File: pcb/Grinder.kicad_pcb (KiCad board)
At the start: 4 copper layers, 48 x 73 mm, 32 parts, among them J1 Conn_01x06, J2 Conn_01x05, J3 Conn_01x04, J4 Conn_02x05_Odd_Even, Q1 2N7002, U1 ADS1232IPW, U2 XC6206P502MR

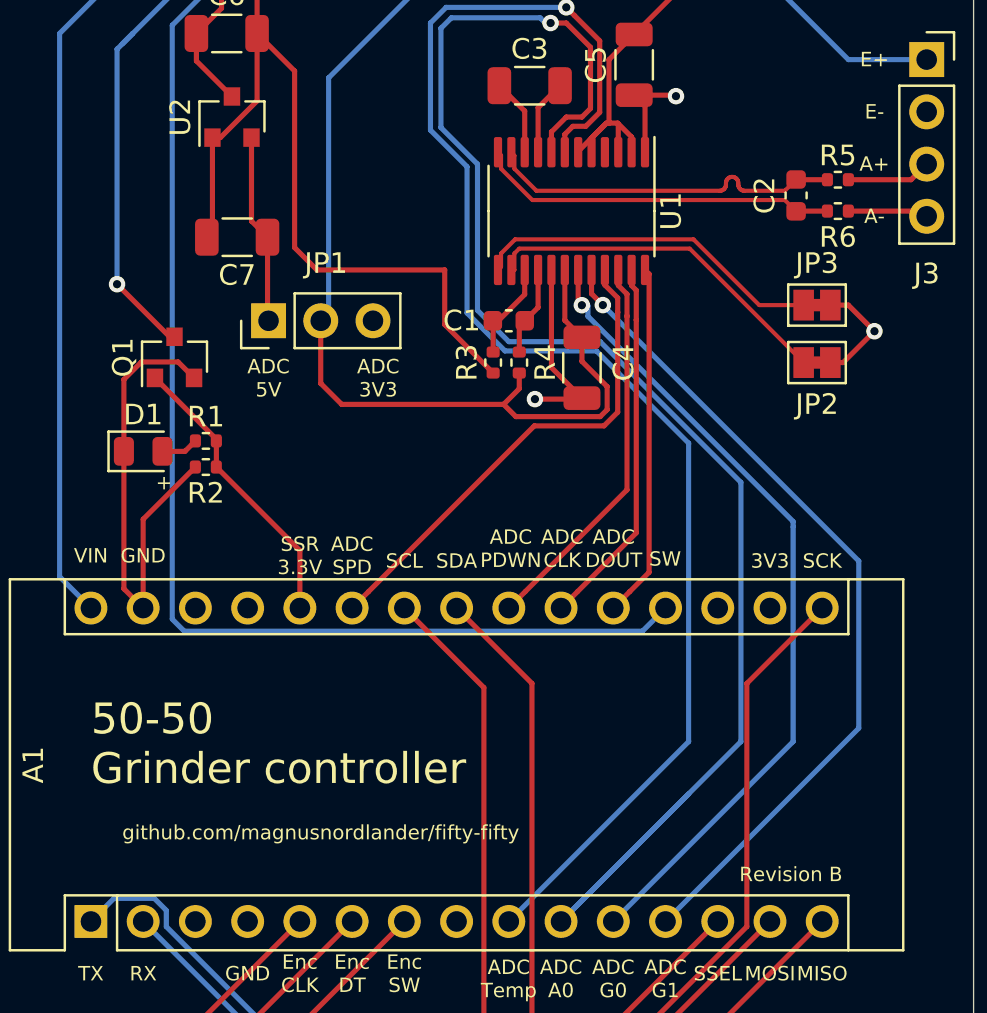
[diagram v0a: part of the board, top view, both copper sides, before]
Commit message: Updated to revision C PCB
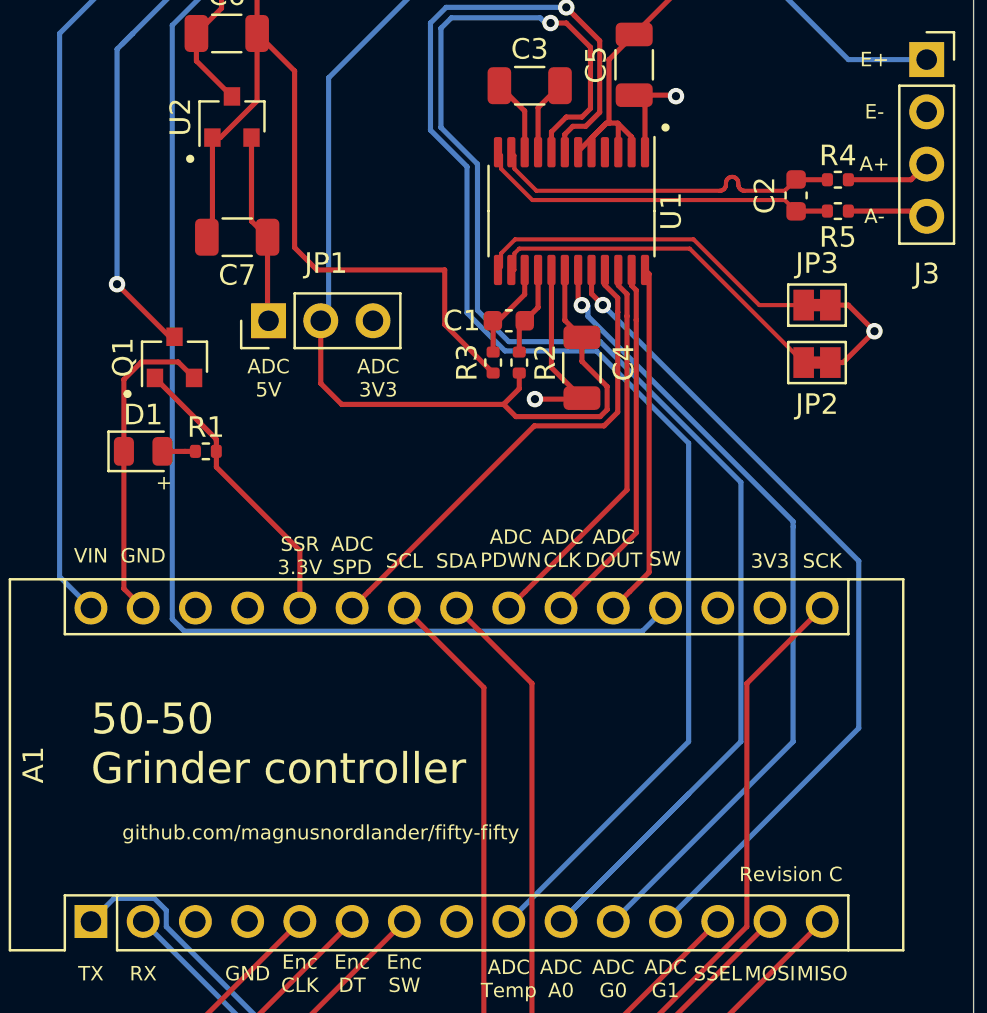
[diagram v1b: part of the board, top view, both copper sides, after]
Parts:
- removed the R2 at (137.7, 78.2)
- moved R1 0.51 mm to (137.7, 77.5)
- renumbered R3 to R2, R4 to R3, R5 to R4, R6 to R5
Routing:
- net GND: track 111.5 -> 103.6 mm
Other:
- board text added: "Revision C"
- board text removed: "Revision B"
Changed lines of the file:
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@@
   (general
     (thickness 1.6)
-    (drawings 89)
-    (tracks 330)
+    (drawings 92)
+    (tracks 328)
     (zones 0)
-    (modules 32)
+    (modules 31)
     (nets 45)
   )
@@
     (tags resistor)
     (attr smd)
-    (fp_text reference R6 (at 0 1.27) (layer F.SilkS)
+    (fp_text reference R5 (at 0 1.27) (layer F.SilkS)
       (effects (font (size 1 1) (thickness 0.15)))
     )
@@
     (tags resistor)
     (attr smd)
-    (fp_text reference R5 (at 0 -1.17) (layer F.SilkS)
+    (fp_text reference R4 (at 0 -1.17) (layer F.SilkS)
       (effects (font (size 1 1) (thickness 0.15)))
     )
@@
     (tags resistor)
     (attr smd)
-    (fp_text reference R4 (at 0 -2.54 90) (layer F.SilkS)
+    (fp_text reference R3 (at 0 1.27 90) (layer F.SilkS)
       (effects (font (size 1 1) (thickness 0.15)))
     )
@@
     (tags resistor)
     (attr smd)
-    (fp_text reference R3 (at 0 2.54 90) (layer F.SilkS)
+    (fp_text reference R2 (at 0 -1.27 90) (layer F.SilkS)
       (effects (font (size 1 1) (thickness 0.15)))
     )
@@
   )
   (module Resistor_SMD:R_0402_1005Metric placed (layer F.Cu)
-    (at 137.668 78.232)
-    (descr "Resistor SMD 0402 (1005 Metric), square (rectangular) end terminal, IPC_7351 nominal, (Body size source: IPC-SM-782 page 72, https://www.pcb-3d.com/wordpress/wp-content/uploads/ipc-sm-782a_amendment_1_and_2.pdf), generated with kicad-footprint-generator")
-    (tags resistor)
-    (attr smd)
-    (fp_text reference R2 (at 0 1.27) (layer F.SilkS)
-      (effects (font (size 1 1) (thickness 0.15)))
-    )
-    (fp_text value 100R (at 0 1.17) (layer F.Fab)
-      (effects (font (size 1 1) (thickness 0.15)))
-    )
-    (fp_line (start -0.525 0.27) (end -0.525 -0.27) (layer F.Fab) (width 0.1))
-    (fp_line (start -0.525 -0.27) (end 0.525 -0.27) (layer F.Fab) (width 0.1))
-    (fp_line (start 0.525 -0.27) (end 0.525 0.27) (layer F.Fab) (width 0.1))
-    (fp_line (start 0.525 0.27) (end -0.525 0.27) (layer F.Fab) (width 0.1))
-    (fp_line (start -0.153641 -0.38) (end 0.153641 -0.38) (layer F.SilkS) (width 0.12))
-    (fp_line (start -0.153641 0.38) (end 0.153641 0.38) (layer F.SilkS) (width 0.12))
-    (fp_line (start -0.93 0.47) (end -0.93 -0.47) (layer F.CrtYd) (width 0.05))
-    (fp_line (start -0.93 -0.47) (end 0.93 -0.47) (layer F.CrtYd) (width 0.05))
-    (fp_line (start 0.93 -0.47) (end 0.93 0.47) (layer F.CrtYd) (width 0.05))
-    (fp_line (start 0.93 0.47) (end -0.93 0.47) (layer F.CrtYd) (width 0.05))
-    (fp_text user %R (at 0 0) (layer F.Fab)
-      (effects (font (size 0.26 0.26) (thickness 0.04)))
-    )
-    (pad 2 smd roundrect (at 0.51 0) (size 0.54 0.64) (layers F.Cu F.Paste F.Mask) (roundrect_rratio 0.25)
-      (net 8 SSR_GATE))
-    (pad 1 smd roundrect (at -0.51 0) (size 0.54 0.64) (layers F.Cu F.Paste F.Mask) (roundrect_rratio 0.25)
-      (net 4 GND))
-    (model ${KISYS3DMOD}/Resistor_SMD.3dshapes/R_0402_1005Metric.wrl
-      (at (xyz 0 0 0))
-      (scale (xyz 1 1 1))
-      (rotate (xyz 0 0 0))
-    )
-  )
-  (module Resistor_SMD:R_0402_1005Metric placed (layer F.Cu)
-    (at 137.67 76.962)
+    (at 137.668 77.47)
     (descr "Resistor SMD 0402 (1005 Metric), square (rectangular) end terminal, IPC_7351 nominal, (Body size source: IPC-SM-782 page 72, https://www.pcb-3d.com/wordpress/wp-content/uploads/ipc-sm-782a_amendment_1_and_2.pdf), generated with kicad-footprint-generator")
     (tags resistor)
@@
     )
   )
-  (gr_text "Revision B" (at 166.116 98.044) (layer F.SilkS)
+  (gr_circle (center 133.858 74.676) (end 133.958 74.676) (layer F.SilkS) (width 0.2))
+  (gr_circle (center 136.906 63.246) (end 137.006 63.246) (layer F.SilkS) (width 0.2))
+  (gr_circle (center 160.02 61.722) (end 160.12 61.722) (layer F.SilkS) (width 0.2))
+  (gr_text "Revision C" (at 166.116 98.044) (layer F.SilkS)
     (effects (font (size 0.7 0.7) (thickness 0.1)))
   )
@@
     (effects (font (size 1.5 1.5) (thickness 0.3)) (justify left))
   )
-  (gr_text "FB 20" (at 168.91 74.676) (layer Cmts.User)
+  (gr_text "FB 20" (at 169.164 77.47) (layer Cmts.User)
     (effects (font (size 1.5 1.5) (thickness 0.3)))
   )
@@
   (segment (start 158.75 114.3) (end 157.574999 113.124999) (width 0.25) (layer F.Cu) (net 3))
   (segment (start 133.6825 84.1525) (end 134.62 85.09) (width 0.25) (layer F.Cu) (net 4))
-  (segment (start 134.62 80.77) (end 137.158 78.232) (width 0.25) (layer F.Cu) (net 4))
-  (segment (start 134.62 85.09) (end 134.62 80.77) (width 0.25) (layer F.Cu) (net 4))
   (segment (start 133.6825 77.47) (end 133.6825 84.1525) (width 0.25) (layer F.Cu) (net 4))
   (segment (start 140.159 51.611) (end 143.51 48.26) (width 0.25) (layer F.Cu) (net 4))
@@
   (segment (start 153.823 60.758) (end 154.891 59.69) (width 0.25) (layer F.Cu) (net 29))
   (segment (start 153.823 62.9235) (end 153.823 60.758) (width 0.25) (layer F.Cu) (net 29))
-  (segment (start 136.652 77.47) (end 137.16 76.962) (width 0.25) (layer F.Cu) (net 31))
   (segment (start 135.5575 77.47) (end 136.652 77.47) (width 0.25) (layer F.Cu) (net 31))
+  (segment (start 136.652 77.47) (end 137.158 77.47) (width 0.25) (layer F.Cu) (net 31))
   (segment (start 151.625 71.12) (end 151.638 71.12) (width 0.25) (layer F.Cu) (net 32))
   (segment (start 151.638 71.133) (end 151.625 71.12) (width 0.25) (layer F.Cu) (net 32))
